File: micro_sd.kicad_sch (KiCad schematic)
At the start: 9 parts, among them J10 Micro_SD_Card

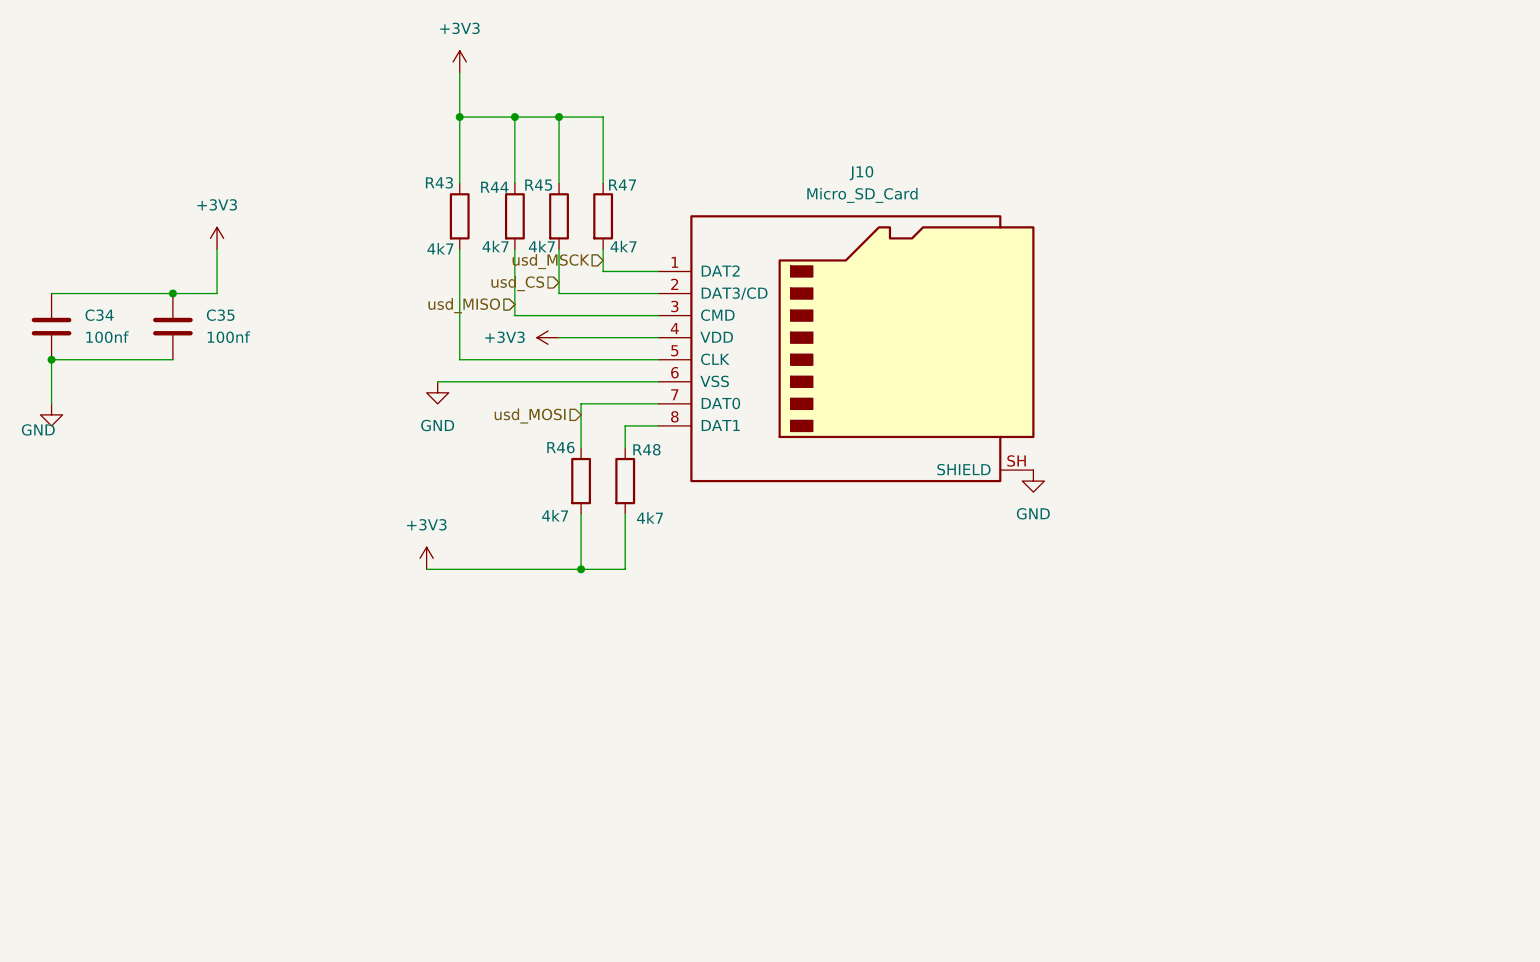
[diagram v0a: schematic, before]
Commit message: Actualización de esquema y PCB del proyecto ESP32C6 Xiaozhi
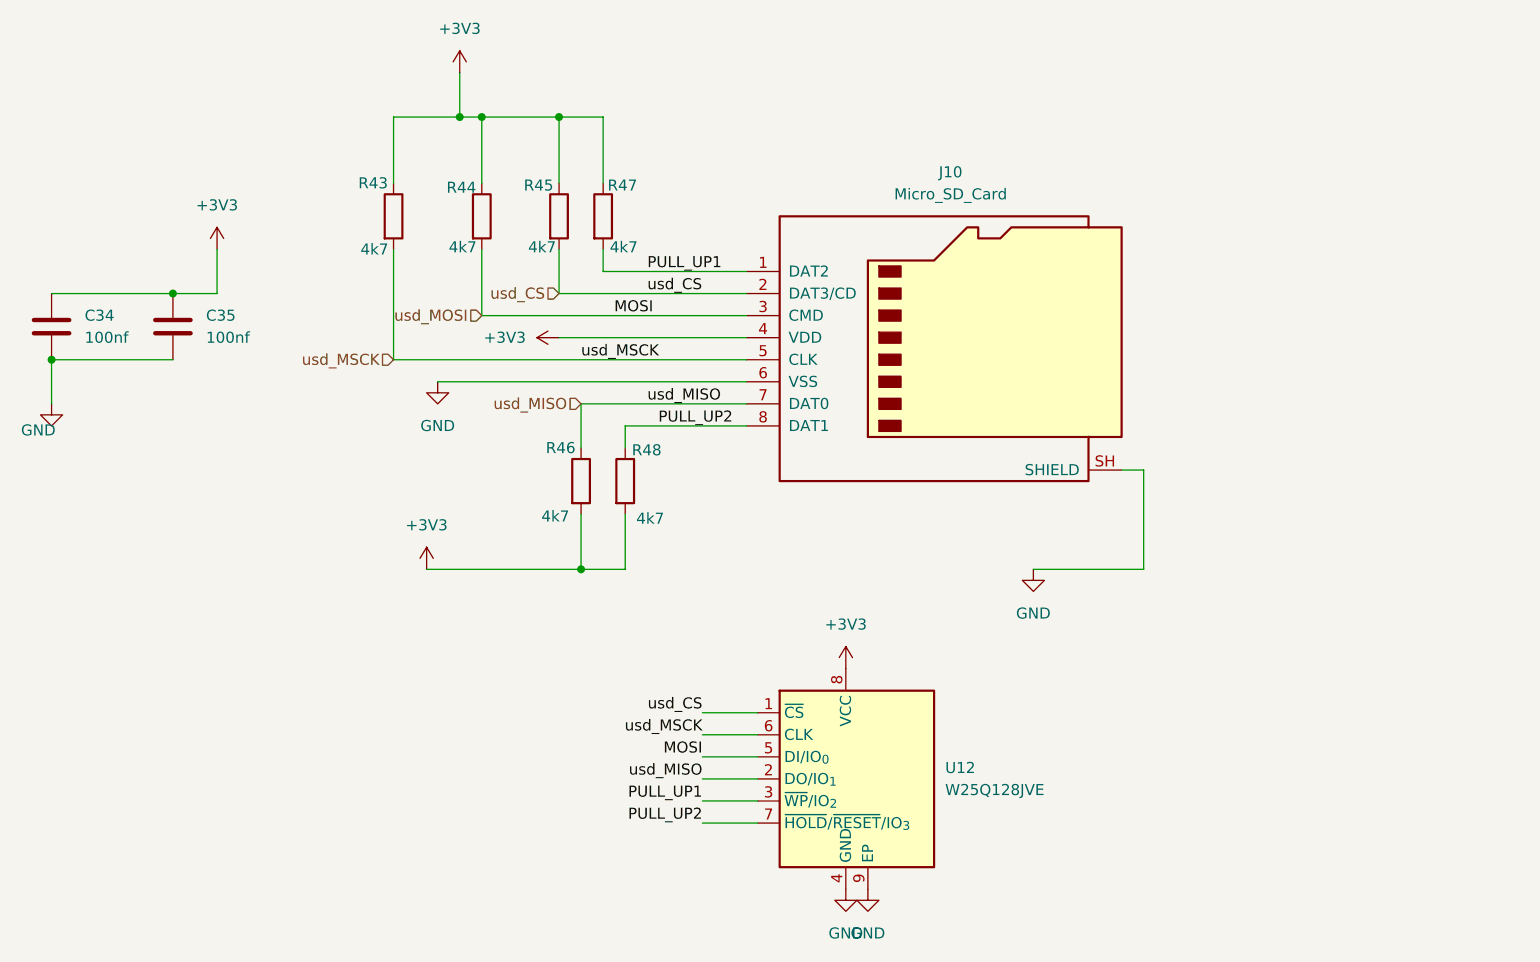
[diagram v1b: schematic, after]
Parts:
- added U12: W25Q128JVE, Package_SON:WSON-8-1EP_8x6mm_P1.27mm_EP3.4x4.3mm, symbol Memory_Flash:W25Q128JVE
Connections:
- net +3V3: now also U12.8 (VCC)
- net GND: now also U12.4 (GND), U12.9 (EP)
- net usd_CS: now also U12.1 (~{CS})
- net usd_MISO: now also J10.7 (DAT0), R46.1, U12.2 (DO/IO_{1}); no longer J10.3 (CMD), R44.2
- net usd_MOSI: now also J10.3 (CMD), R44.2, U12.5 (DI/IO_{0}); no longer J10.7 (DAT0), R46.1
- net usd_MSCK: now also J10.5 (CLK), R43.2, U12.6 (CLK); no longer J10.1 (DAT2), R47.2
- net PULL_UP2: now reaches J10.8 (DAT1), R48.1
- net PULL_UP2: now also U12.7 (~{HOLD}/~{RESET}/IO_{3})
- new net PULL_UP1: J10.1 (DAT2), R47.2, U12.3 (~{WP}/IO_{2})
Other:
- moved on the sheet: J10, R43, R44

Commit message: Update KiCad PCB, project, and micro_sd schematic
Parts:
- added U10: W25Q128JVSIQ, RaspberryPI PicoW:generic_soic127p790x195-8, symbol RPI_DB:Integrated_Circuits | Memory | Serial_Flash | SPI/RP-01JWD4-F1H4N9
- U12: footprint Package_SON:WSON-8-1EP_8x6mm_P1.27mm_EP3.4x4.3mm -> kiC:Winbond_XSON-8-1EP_4x4mm_P0.8mm_EP2.3x3.0mm
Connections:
- net +3V3: now also U10.8 (VCC)
- net GND: now also U10.4 (GND)
- net PULL_UP1: now also U10.3 (~{WP}_IO2)
- net PULL_UP2: now also U10.7 (~{HOLD}_IO3)
- net usd_CS: now also U10.1 (~{CS})
- net usd_MISO: now also U10.2 (DO_IO1)
- net usd_MOSI: now also U10.5 (DI_IO0)
- net usd_MSCK: now also U10.6 (CLK)

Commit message: add files update
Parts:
- U12: now left out of the parts list
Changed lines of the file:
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@@
 		(body_style 1)
 		(exclude_from_sim no)
-		(in_bom yes)
+		(in_bom no)
 		(on_board yes)
-		(in_pos_files yes)
+		(in_pos_files no)
 		(dnp no)
 		(fields_autoplaced yes)

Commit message: Actualización de esquemas y PCB con datos LCSC y librerías JLC
- Añade propiedades LCSC a los símbolos de las hojas de esquema
- Actualiza las hojas TXS0108E, display, esp32_c6, ft232, inmp441,
  led_sw_gpio, max98357a, micro_sd, power_supply y el esquema raíz
- Reorganiza el PCB (footprints, jumpers y nets) y actualiza el proyecto
- Incluye las librerías locales JLCImport (símbolos, huellas y modelos 3D)
  y las entradas correspondientes en fp-lib-table y sym-lib-table
- Añade la documentación técnica en docs/ y el archivo de posiciones
  esp32_xiaozhi-all.pos
- Elimina los ZIP generados gebers.zip y production.zip
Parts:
- C34, C35: LCSC (none) -> C1525
- J10: LCSC (none) -> C125617
- R43, R44, R45, R46, R47, R48: LCSC (none) -> C17673
- U10: footprint RaspberryPI PicoW:generic_soic127p790x195-8 -> kiC:SOIC-8W_5.3x5.3mm_P1.27mm; LCSC (none) -> C97521; manufacturer Winbond -> (none); package SOIC-8 -> (none)
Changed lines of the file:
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@@
+			)
+		)
+		(property "LCSC" "C17673"
+			(at 121.92 100.33 0)
+			(hide yes)
+			(show_name no)
+			(do_not_autoplace no)
+			(effects
+				(font
+					(size 1.27 1.27)
+				)
 			)
 		)
@@
 			)
 		)
+		(property "LCSC" "C17673"
+			(at 124.46 69.85 0)
+			(hide yes)
+			(show_name no)
+			(do_not_autoplace no)
+			(effects
+				(font
+					(size 1.27 1.27)
+				)
+			)
+		)
 		(pin "1"
 		)
@@
 		(property "Description" ""
 			(at 100.33 69.85 0)
+			(show_name no)
+			(do_not_autoplace no)
+			(effects
+				(font
+					(size 1.27 1.27)
+				)
+			)
+		)
+		(property "LCSC" "C17673"
+			(at 100.33 69.85 0)
+			(hide yes)
 			(show_name no)
 			(do_not_autoplace no)
@@
 			)
 		)
-		(property "Footprint" "RaspberryPI PicoW:generic_soic127p790x195-8"
+		(property "Footprint" "kiC:SOIC-8W_5.3x5.3mm_P1.27mm"
 			(at 217.17 125.095 0)
 			(hide yes)
@@
 			)
 		)
-		(property "manufacturer" "Winbond"
-			(at 215.9 133.35 0)
-			(hide yes)
-			(show_name no)
-			(do_not_autoplace no)
-			(effects
-				(font
-					(size 1.27 1.27)
-				)
-			)
-		)
 		(property "manufacturer_pn" "W25Q128JVSIQ"
 			(at 215.9 133.35 0)
@@
 			)
 		)
-		(property "package" "SOIC-8"
-			(at 215.9 133.35 0)
-			(hide yes)
-			(show_name no)
-			(do_not_autoplace no)
-			(effects
-				(font
-					(size 1.27 1.27)
-				)
-			)
-		)
 		(property "z_height_nom" "1.95mm"
 			(at 215.9 133.35 0)
@@
 			)
 		)
+		(property "LCSC" "C97521"
+			(at 215.9 133.35 0)
+			(hide yes)
+			(show_name no)
+			(do_not_autoplace no)
+			(effects
+				(font
+					(size 1.27 1.27)
+				)
+			)
+		)
 		(pin "1"
 		)
@@
 		(property "Description" ""
 			(at 127 100.33 0)
+			(show_name no)
+			(do_not_autoplace no)
+			(effects
+				(font
+					(size 1.27 1.27)
+				)
+			)
+		)
+		(property "LCSC" "C17673"
+			(at 127 100.33 0)
+			(hide yes)
 			(show_name no)
 			(do_not_autoplace no)
@@
 			)
 		)
+		(property "LCSC" "C17673"
+			(at 110.49 69.85 0)
+			(hide yes)
+			(show_name no)
+			(do_not_autoplace no)
+			(effects
+				(font
+					(size 1.27 1.27)
+				)
+			)
+		)
 		(pin "1"
 		)
@@
 			)
 		)
+		(property "LCSC" "C17673"
+			(at 119.38 69.85 0)
+			(hide yes)
+			(show_name no)
+			(do_not_autoplace no)
+			(effects
+				(font
+					(size 1.27 1.27)
+				)
+			)
+		)
 		(pin "1"
 		)
@@
 			)
 		)
+		(property "LCSC" "C125617"
+			(at 163.83 83.82 0)
+			(hide yes)
+			(show_name no)
+			(do_not_autoplace no)
+			(effects
+				(font
+					(size 1.27 1.27)
+				)
+			)
+		)
 		(pin "1"
 		)
@@
 			)
 		)
+		(property "LCSC" "C1525"
+			(at 60.96 82.55 0)
+			(hide yes)
+			(show_name no)
+			(do_not_autoplace no)
+			(effects
+				(font
+					(size 1.27 1.27)
+				)
+			)
+		)
 		(pin "1"
 		)
@@
 			(show_name no)
 			(do_not_autoplace no)
+			(effects
+				(font
+					(size 1.27 1.27)
+				)
+			)
+		)
+		(property "LCSC" "C1525"
+			(at 74.93 82.55 0)
+			(hide yes)
+			(show_name no)
+			(do_not_autoplace no)

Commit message: Actualización de esquemas, PCB y librerías
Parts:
- C34, C35: LCSC C1525 -> C28233
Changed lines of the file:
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@@
 			)
 		)
-		(property "LCSC" "C1525"
+		(property "LCSC" "C28233"
 			(at 60.96 82.55 0)
 			(hide yes)
@@
 			)
 		)
-		(property "LCSC" "C1525"
+		(property "LCSC" "C28233"
 			(at 74.93 82.55 0)
 			(hide yes)

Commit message: correccion de partes
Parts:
- J10: value Micro_SD_Card -> TF-001B; footprint Library:3M_2908-05WB-MG -> JLCImport:TF-001B
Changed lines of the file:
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@@
 			)
 		)
-		(property "Value" "Micro_SD_Card"
+		(property "Value" "TF-001B"
 			(at 164.465 67.31 0)
 			(show_name no)
@@
 			)
 		)
-		(property "Footprint" "Library:3M_2908-05WB-MG"
+		(property "Footprint" "JLCImport:TF-001B"
 			(at 193.04 76.2 0)
 			(hide yes)
